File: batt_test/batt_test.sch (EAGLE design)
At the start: 1 part, among them U1 PHOTON

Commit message: start  board layout
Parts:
- added D1: RED, scono:LED0603
- added D3: BLUE, scono:LED0603
- added D4: GREEN, scono:LED0603
- added D5: YELLOW, scono:LED0603
- added D6: WHITE, scono:LED0603
- added J1: UART, scono:CONN_02
- added R1: 10R, scono:R-US_R0603
- added R2, R3, R4, R5, R6: 330, BEST_Custom:R-US_R0402
- added TP1, TP2: TEST_POINT, scono:TEST_POINT
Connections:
- new net B+: R1.1, TP2.P$1, U1.A3
- new net B-: R1.2, TP1.P$1, U1.A5, U1.DAC
- new net BLUE: R3.2, U1.D3
- new net GND: D1.C, D3.C, D4.C, D5.C, D6.C, U1.GND
- new net GREEN: R4.2, U1.D2
- new net N$11: D5.A, R5.1
- new net N$12: D6.A, R6.1
- new net N$6: D1.A, R2.1
- new net N$8: D3.A, R3.1
- new net N$9: D4.A, R4.1
- new net RED: R2.2, U1.D4
- new net RX: J1.1, U1.RX
- new net TX: J1.2, U1.TX
- new net WHITE: R6.2, U1.D0
- new net YELLOW: R5.2, U1.D1
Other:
- moved on the sheet: U1

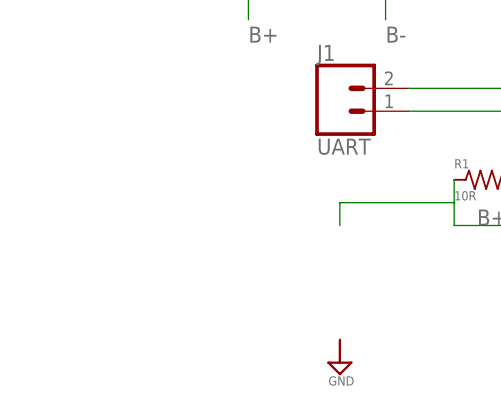
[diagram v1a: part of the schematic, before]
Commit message: add batt test point
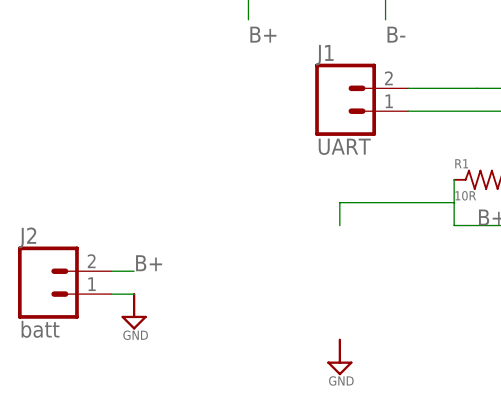
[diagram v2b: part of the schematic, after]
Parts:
- added J2: batt, scono:CONN_02
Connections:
- net B+: now also J2.2
- net GND: now also J2.1
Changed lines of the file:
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@@
 <part name="TP2" library="scono" deviceset="TEST_POINT" device=""/>
 <part name="J1" library="scono" deviceset="CONN_02" device="" package3d_urn="urn:adsk.eagle:package:38039/1" value="UART"/>
+<part name="J2" library="scono" deviceset="CONN_02" device="" package3d_urn="urn:adsk.eagle:package:38039/1" value="batt"/>
+<part name="SUPPLY4" library="scono" deviceset="GND" device=""/>
 </parts>
 <sheets>
@@
 <attribute name="NAME" x="78.74" y="112.268" size="1.778" layer="95" font="vector"/>
 </instance>
+<instance part="J2" gate="G$1" x="48.26" y="86.36" smashed="yes">
+<attribute name="VALUE" x="45.72" y="81.534" size="1.778" layer="96" font="vector"/>
+<attribute name="NAME" x="45.72" y="91.948" size="1.778" layer="95" font="vector"/>
+</instance>
+<instance part="SUPPLY4" gate="GND" x="58.42" y="83.82" smashed="yes">
+<attribute name="VALUE" x="57.15" y="81.28" size="1.016" layer="96"/>
+</instance>
 </instances>
 <busses>
@@
 <label x="71.12" y="114.3" size="1.778" layer="95"/>
 </segment>
+<segment>
+<pinref part="J2" gate="G$1" pin="2"/>
+<wire x1="55.88" y1="88.9" x2="58.42" y2="88.9" width="0.1524" layer="91"/>
+<label x="58.42" y="88.9" size="1.778" layer="95"/>
+</segment>
 </net>
 <net name="GND" class="0">
@@
 <junction x="170.18" y="83.82"/>
 </segment>
+<segment>
+<pinref part="J2" gate="G$1" pin="1"/>
+<wire x1="55.88" y1="86.36" x2="58.42" y2="86.36" width="0.1524" layer="91"/>
+<pinref part="SUPPLY4" gate="GND" pin="GND"/>
+</segment>
 </net>

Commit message: finish first proto
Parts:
- added B1: 2020COINCELL, scono:2020COINCELL
- renumbered TP1 to B-, TP2 to POS
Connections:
- net B+: now also B1.POS
- net GND: now also B1.NEG
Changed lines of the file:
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@@
 <part name="SUPPLY2" library="scono" deviceset="GND" device=""/>
 <part name="SUPPLY3" library="scono" deviceset="GND" device=""/>
-<part name="TP1" library="scono" deviceset="TEST_POINT" device=""/>
-<part name="TP2" library="scono" deviceset="TEST_POINT" device=""/>
+<part name="B-" library="scono" deviceset="TEST_POINT" device=""/>
+<part name="POS" library="scono" deviceset="TEST_POINT" device=""/>
 <part name="J1" library="scono" deviceset="CONN_02" device="" package3d_urn="urn:adsk.eagle:package:38039/1" value="UART"/>
 <part name="J2" library="scono" deviceset="CONN_02" device="" package3d_urn="urn:adsk.eagle:package:38039/1" value="batt"/>
 <part name="SUPPLY4" library="scono" deviceset="GND" device=""/>
+<part name="B1" library="scono" deviceset="2020COINCELL" device=""/>
 </parts>
 <sheets>
@@
 <attribute name="VALUE" x="80.01" y="76.2" size="1.016" layer="96"/>
 </instance>
-<instance part="TP1" gate="G$1" x="86.36" y="127" smashed="yes" rot="R90">
+<instance part="B-" gate="G$1" x="86.36" y="127" smashed="yes" rot="R90">
 <attribute name="NAME" x="82.55" y="123.19" size="1.778" layer="104" rot="R90"/>
 </instance>
-<instance part="TP2" gate="G$1" x="71.12" y="127" smashed="yes" rot="R90">
+<instance part="POS" gate="G$1" x="71.12" y="127" smashed="yes" rot="R90">
 <attribute name="NAME" x="67.31" y="123.19" size="1.778" layer="104" rot="R90"/>
 </instance>
@@
 <instance part="SUPPLY4" gate="GND" x="58.42" y="83.82" smashed="yes">
 <attribute name="VALUE" x="57.15" y="81.28" size="1.016" layer="96"/>
+</instance>
+<instance part="B1" gate="G$1" x="81.28" y="88.9" smashed="yes">
+<attribute name="NAME" x="73.66" y="81.28" size="3.2512" layer="95" font="vector" rot="R90"/>
 </instance>
 </instances>
@@
 </segment>
 <segment>
-<pinref part="TP1" gate="G$1" pin="P$1"/>
+<pinref part="B-" gate="G$1" pin="P$1"/>
 <wire x1="86.36" y1="119.38" x2="86.36" y2="116.84" width="0.1524" layer="91"/>
 <label x="86.36" y="114.3" size="1.778" layer="95"/>
@@
 <wire x1="93.98" y1="96.52" x2="81.28" y2="96.52" width="0.1524" layer="91"/>
 <wire x1="81.28" y1="96.52" x2="81.28" y2="93.98" width="0.1524" layer="91"/>
+<pinref part="B1" gate="G$1" pin="POS"/>
 </segment>
 <segment>
-<pinref part="TP2" gate="G$1" pin="P$1"/>
+<pinref part="POS" gate="G$1" pin="P$1"/>
 <wire x1="71.12" y1="119.38" x2="71.12" y2="116.84" width="0.1524" layer="91"/>
 <label x="71.12" y="114.3" size="1.778" layer="95"/>
@@
 <pinref part="SUPPLY4" gate="GND" pin="GND"/>
 </segment>
+<segment>
+<pinref part="SUPPLY3" gate="GND" pin="GND"/>
+<pinref part="B1" gate="G$1" pin="NEG"/>
+</segment>
 </net>

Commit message: update bom and gerber
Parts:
- removed J1: UART, scono:CONN_02
- removed J2: batt, scono:CONN_02
- added B+, TP2: TEST_POINTTHRU, scono:TEST_POINTTHRU
- added U2: 1101M2S3CQE2, scono:1101M2S3CQE2
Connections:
- removed net RX: J1.1, U1.RX
- removed net TX: J1.2, U1.TX
- new net N$1: B1.NEG, U2.1
- net B+: now also B+.P$1; no longer J2.2
- net GND: now also TP2.P$1, U2.2; no longer B1.NEG, J2.1
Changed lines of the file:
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@@
 <?xml version="1.0" encoding="utf-8"?>
 <!DOCTYPE eagle SYSTEM "eagle.dtd">
-<eagle version="9.3.1">
+<eagle version="9.3.2">
 <drawing>
 <settings>
@@
 <part name="B-" library="scono" deviceset="TEST_POINT" device=""/>
 <part name="POS" library="scono" deviceset="TEST_POINT" device=""/>
-<part name="J1" library="scono" deviceset="CONN_02" device="" package3d_urn="urn:adsk.eagle:package:38039/1" value="UART"/>
-<part name="J2" library="scono" deviceset="CONN_02" device="" package3d_urn="urn:adsk.eagle:package:38039/1" value="batt"/>
 <part name="SUPPLY4" library="scono" deviceset="GND" device=""/>
 <part name="B1" library="scono" deviceset="2020COINCELL" device=""/>
+<part name="U2" library="scono" deviceset="1101M2S3CQE2" device=""/>
+<part name="B+" library="scono" deviceset="TEST_POINT" device="THRU"/>
+<part name="TP2" library="scono" deviceset="TEST_POINT" device="THRU"/>
 </parts>
 <sheets>
@@
 <attribute name="VALUE" x="168.91" y="78.74" size="1.016" layer="96"/>
 </instance>
-<instance part="SUPPLY3" gate="GND" x="81.28" y="78.74" smashed="yes">
-<attribute name="VALUE" x="80.01" y="76.2" size="1.016" layer="96"/>
+<instance part="SUPPLY3" gate="GND" x="55.88" y="55.88" smashed="yes">
+<attribute name="VALUE" x="54.61" y="53.34" size="1.016" layer="96"/>
 </instance>
 <instance part="B-" gate="G$1" x="86.36" y="127" smashed="yes" rot="R90">
 <attribute name="NAME" x="82.55" y="123.19" size="1.778" layer="104" rot="R90"/>
 </instance>
-<instance part="POS" gate="G$1" x="71.12" y="127" smashed="yes" rot="R90">
-<attribute name="NAME" x="67.31" y="123.19" size="1.778" layer="104" rot="R90"/>
-</instance>
-<instance part="J1" gate="G$1" x="81.28" y="106.68" smashed="yes">
-<attribute name="VALUE" x="78.74" y="101.854" size="1.778" layer="96" font="vector"/>
-<attribute name="NAME" x="78.74" y="112.268" size="1.778" layer="95" font="vector"/>
-</instance>
-<instance part="J2" gate="G$1" x="48.26" y="86.36" smashed="yes">
-<attribute name="VALUE" x="45.72" y="81.534" size="1.778" layer="96" font="vector"/>
-<attribute name="NAME" x="45.72" y="91.948" size="1.778" layer="95" font="vector"/>
-</instance>
-<instance part="SUPPLY4" gate="GND" x="58.42" y="83.82" smashed="yes">
-<attribute name="VALUE" x="57.15" y="81.28" size="1.016" layer="96"/>
+<instance part="POS" gate="G$1" x="76.2" y="127" smashed="yes" rot="R90">
+<attribute name="NAME" x="72.39" y="123.19" size="1.778" layer="104" rot="R90"/>
+</instance>
+<instance part="SUPPLY4" gate="GND" x="58.42" y="81.28" smashed="yes" rot="R90">
+<attribute name="VALUE" x="60.96" y="80.01" size="1.016" layer="96" rot="R90"/>
 </instance>
 <instance part="B1" gate="G$1" x="81.28" y="88.9" smashed="yes">
 <attribute name="NAME" x="73.66" y="81.28" size="3.2512" layer="95" font="vector" rot="R90"/>
+</instance>
+<instance part="U2" gate="A" x="68.58" y="58.42" smashed="yes">
+<attribute name="NAME" x="61.3156" y="72.6186" size="2.0828" layer="95" ratio="6" rot="SR0"/>
+<attribute name="VALUE" x="60.6806" y="42.1386" size="2.0828" layer="96" ratio="6" rot="SR0"/>
+</instance>
+<instance part="B+" gate="G$1" x="55.88" y="88.9" smashed="yes" rot="R180">
+<attribute name="NAME" x="55.88" y="86.36" size="1.778" layer="104" rot="R180"/>
+</instance>
+<instance part="TP2" gate="G$1" x="55.88" y="81.28" smashed="yes" rot="R180">
+<attribute name="NAME" x="55.88" y="78.74" size="1.778" layer="104" rot="R180"/>
 </instance>
 </instances>
@@
 <segment>
 <pinref part="B-" gate="G$1" pin="P$1"/>
-<wire x1="86.36" y1="119.38" x2="86.36" y2="116.84" width="0.1524" layer="91"/>
+<wire x1="86.36" y1="127" x2="86.36" y2="116.84" width="0.1524" layer="91"/>
 <label x="86.36" y="114.3" size="1.778" layer="95"/>
 </segment>
@@
 <segment>
 <pinref part="POS" gate="G$1" pin="P$1"/>
-<wire x1="71.12" y1="119.38" x2="71.12" y2="116.84" width="0.1524" layer="91"/>
-<label x="71.12" y="114.3" size="1.778" layer="95"/>
-</segment>
-<segment>
-<pinref part="J2" gate="G$1" pin="2"/>
+<wire x1="76.2" y1="127" x2="76.2" y2="116.84" width="0.1524" layer="91"/>
+<label x="76.2" y="114.3" size="1.778" layer="95"/>
+</segment>
+<segment>
 <wire x1="55.88" y1="88.9" x2="58.42" y2="88.9" width="0.1524" layer="91"/>
 <label x="58.42" y="88.9" size="1.778" layer="95"/>
+<pinref part="B+" gate="G$1" pin="P$1"/>
 </segment>
 </net>
@@
 </segment>
 <segment>
-<pinref part="J2" gate="G$1" pin="1"/>
-<wire x1="55.88" y1="86.36" x2="58.42" y2="86.36" width="0.1524" layer="91"/>
 <pinref part="SUPPLY4" gate="GND" pin="GND"/>
-</segment>
-<segment>
+<pinref part="TP2" gate="G$1" pin="P$1"/>
+</segment>
+<segment>
+<pinref part="U2" gate="A" pin="2"/>
 <pinref part="SUPPLY3" gate="GND" pin="GND"/>
-<pinref part="B1" gate="G$1" pin="NEG"/>
+<wire x1="55.88" y1="58.42" x2="58.42" y2="58.42" width="0.1524" layer="91"/>
 </segment>
 </net>
@@
 </segment>
 </net>
-<net name="TX" class="0">
-<segment>
-<pinref part="U1" gate="G$1" pin="TX"/>
-<wire x1="104.14" y1="109.22" x2="101.6" y2="109.22" width="0.1524" layer="91"/>
-<label x="101.6" y="109.22" size="1.778" layer="95"/>
-<pinref part="J1" gate="G$1" pin="2"/>
-<wire x1="88.9" y1="109.22" x2="96.52" y2="109.22" width="0.1524" layer="91"/>
-<wire x1="101.6" y1="109.22" x2="96.52" y2="109.22" width="0.1524" layer="91"/>
-</segment>
-</net>
-<net name="RX" class="0">
-<segment>
-<pinref part="U1" gate="G$1" pin="RX"/>
-<label x="101.6" y="106.68" size="1.778" layer="95"/>
-<pinref part="J1" gate="G$1" pin="1"/>
-<wire x1="104.14" y1="106.68" x2="88.9" y2="106.68" width="0.1524" layer="91"/>
+<net name="N$1" class="0">
+<segment>
+<pinref part="B1" gate="G$1" pin="NEG"/>
+<wire x1="81.28" y1="63.5" x2="81.28" y2="81.28" width="0.1524" layer="91"/>
+<pinref part="U2" gate="A" pin="1"/>
+<wire x1="81.28" y1="63.5" x2="78.74" y2="63.5" width="0.1524" layer="91"/>
 </segment>
 </net>
@@
 </schematic>
 </drawing>
-<compatibility>
-<note version="8.3" severity="warning">
-Since Version 8.3, EAGLE supports URNs for individual library
-assets (packages, symbols, and devices). The URNs of those assets
-will not be understood (or retained) with this version.
-</note>
-<note version="8.3" severity="warning">
-Since Version 8.3, EAGLE supports the association of 3D packages
-with devices in libraries, schematics, and board files. Those 3D
-packages will not be understood (or retained) with this version.
-</note>
-</compatibility>
 </eagle>

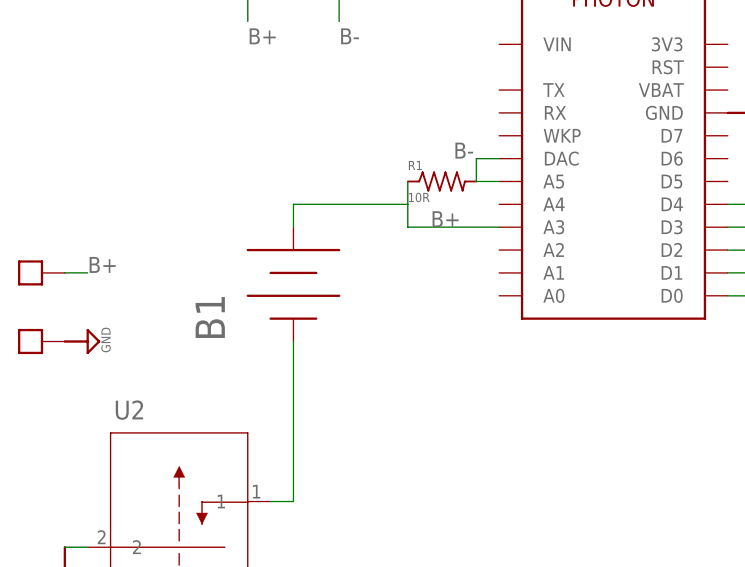
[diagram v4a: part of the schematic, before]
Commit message: new contacts and bom
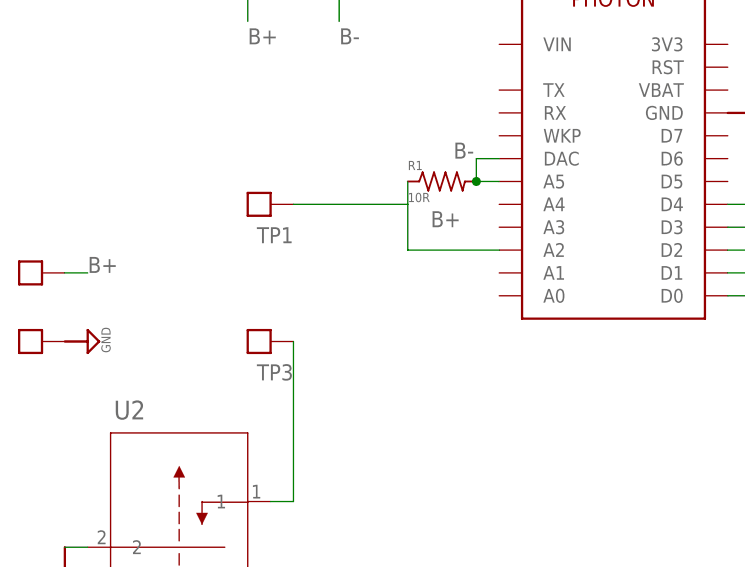
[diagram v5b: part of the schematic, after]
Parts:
- removed B1: 2020COINCELL, scono:2020COINCELL
- added TP1, TP3: TEST_POINTTHRU, scono:TEST_POINTTHRU
- R1: device scono:R-US_R0603 -> scono:R-US_R0805
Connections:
- net B+: now also TP1.P$1, U1.A2; no longer B1.POS, U1.A3
- net N$1: now also TP3.P$1; no longer B1.NEG

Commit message: one last time?
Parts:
- added B-2: TEST_POINTTHRU, scono:TEST_POINTTHRU
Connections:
- net B-: now also B-2.P$1
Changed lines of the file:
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@@
 <?xml version="1.0" encoding="utf-8"?>
 <!DOCTYPE eagle SYSTEM "eagle.dtd">
-<eagle version="9.4.0">
+<eagle version="9.5.2">
 <drawing>
 <settings>
-<setting alwaysvectorfont="no"/>
+<setting alwaysvectorfont="yes"/>
 <setting verticaltext="up"/>
 </settings>
@@
 <part name="TP1" library="scono" deviceset="TEST_POINT" device="THRU"/>
 <part name="TP3" library="scono" deviceset="TEST_POINT" device="THRU"/>
+<part name="B-2" library="scono" deviceset="TEST_POINT" device="THRU"/>
 </parts>
 <sheets>
@@
 <instance part="TP3" gate="G$1" x="81.28" y="81.28" smashed="yes" rot="R180">
 <attribute name="NAME" x="81.28" y="78.74" size="1.778" layer="95" rot="R180"/>
+</instance>
+<instance part="B-2" gate="G$1" x="55.88" y="96.52" smashed="yes" rot="R180">
+<attribute name="NAME" x="55.88" y="93.98" size="1.778" layer="104" rot="R180"/>
 </instance>
 </instances>
@@
 <label x="86.36" y="114.3" size="1.778" layer="95"/>
 </segment>
+<segment>
+<pinref part="B-2" gate="G$1" pin="P$1"/>
+<wire x1="55.88" y1="96.52" x2="58.42" y2="96.52" width="0.1524" layer="91"/>
+<label x="58.42" y="96.52" size="1.778" layer="95"/>
+</segment>
 </net>
